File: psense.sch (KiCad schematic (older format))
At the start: 25 parts, among them J1 USB-micro-b, U1 PAC1720, U2 MCP2221A

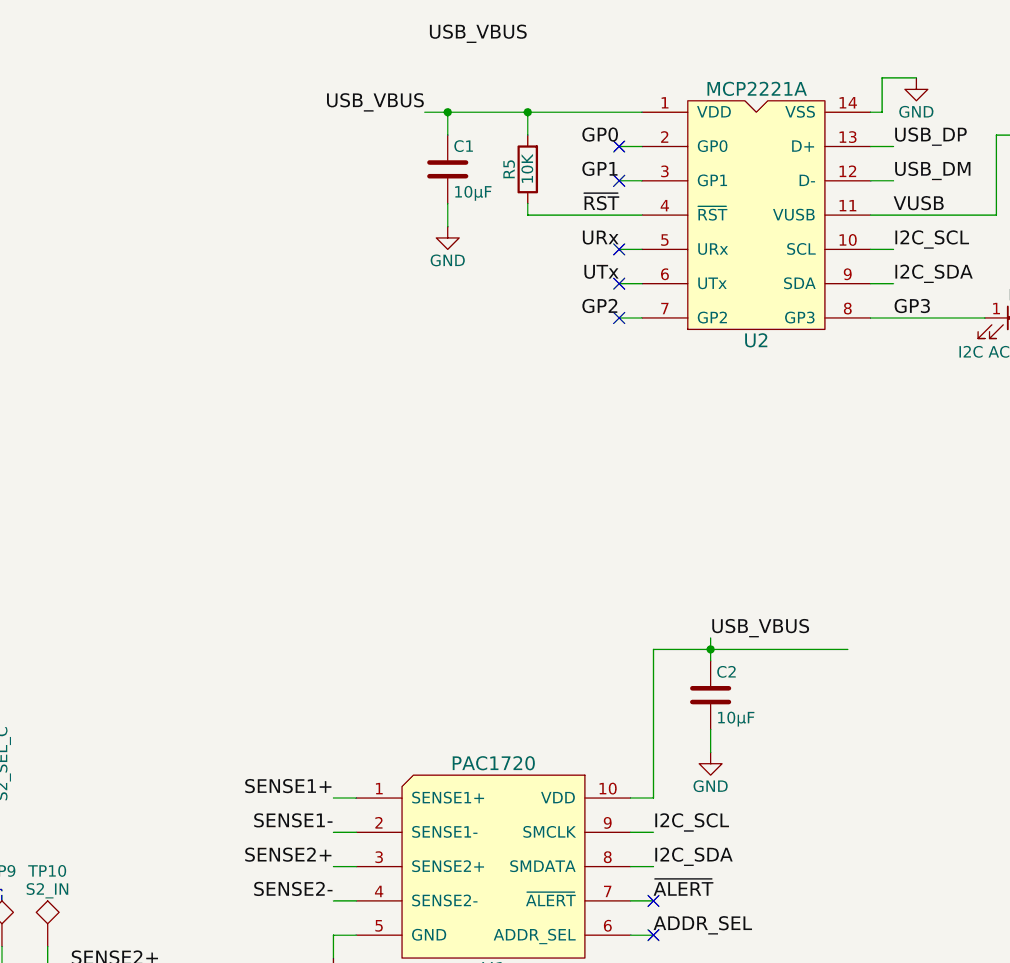
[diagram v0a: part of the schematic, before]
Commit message: Fix https://github.com/noahp/psense/issues/1 https://github.com/noahp/psense/issues/2 https://github.com/noahp/psense/issues/3
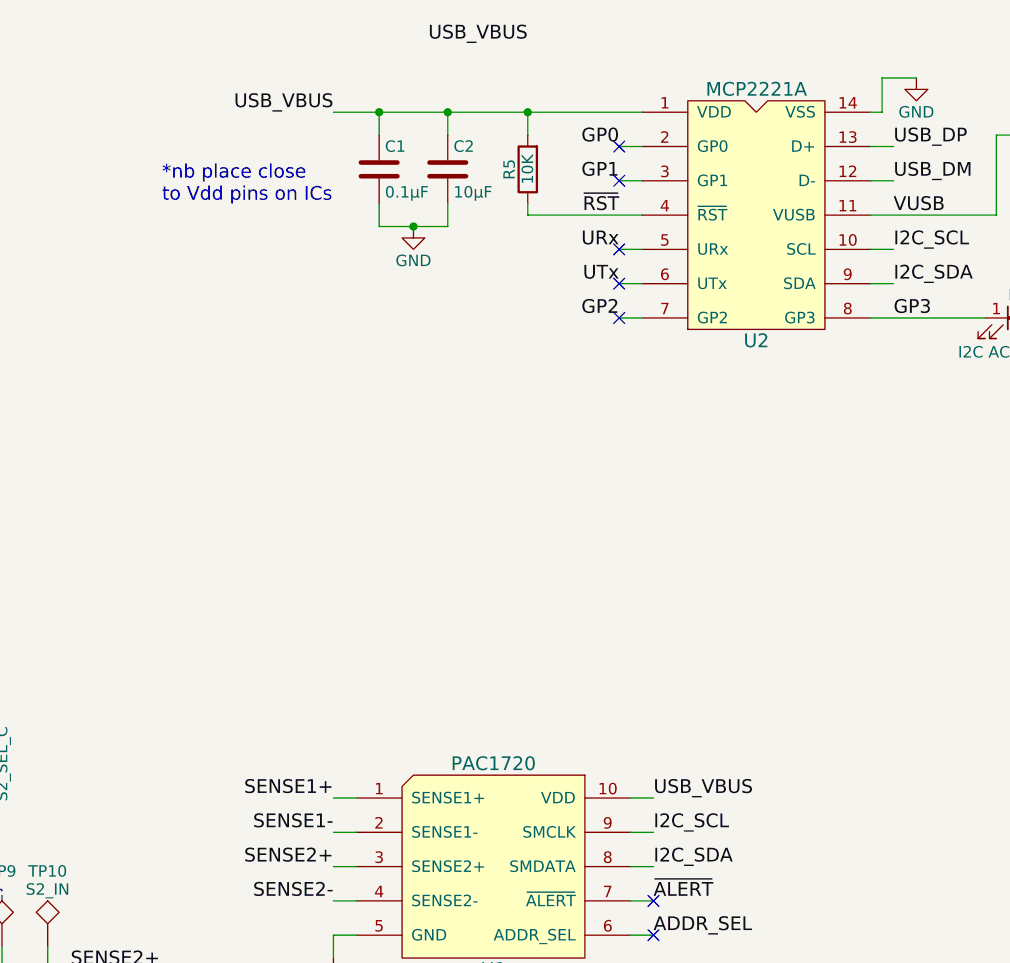
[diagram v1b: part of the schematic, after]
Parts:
- C1: renamed from C2; value 10µF -> 0.1µF
- renumbered C1 to C2
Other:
- note added: "*nb place close\nto Vdd pins on ICs"
- moved on the sheet: C1
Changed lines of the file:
@@
 $EndComp
 $Comp
-L GND #PWR01
+L GND #PWR1
 U 1 1 58A0804C
 P 2700 2700
-F 0 "#PWR01" H 2700 2450 50  0001 C CNN
+F 0 "#PWR1" H 2700 2450 50  0001 C CNN
 F 1 "GND" H 2700 2550 50  0000 C CNN
 F 2 "" H 2700 2700 50  0000 C CNN
@@
 $EndComp
 $Comp
-L GND #PWR02
+L GND #PWR2
 U 1 1 58A09C3A
 P 5150 5200
-F 0 "#PWR02" H 5150 4950 50  0001 C CNN
+F 0 "#PWR2" H 5150 4950 50  0001 C CNN
 F 1 "GND" H 5150 5050 50  0000 C CNN
 F 2 "" H 5150 5200 50  0000 C CNN
@@
 Wire Wire Line
 	6450 4800 6550 4800
-Text Label 6800 3800 0    60   ~ 0
+Text Label 6550 4500 0    60   ~ 0
 USB_VBUS
 $Comp
-L C C2
+L C C1
 U 1 1 58A0A596
-P 6800 4050
-F 0 "C2" H 6825 4150 50  0000 L CNN
-F 1 "10µF" H 6825 3950 50  0000 L CNN
-F 2 "kicadlib:SMD_0603_C" H 6838 3900 50  0001 C CNN
-F 3 "" H 6800 4050 50  0000 C CNN
-	1    6800 4050
-	1    0    0    -1
-$EndComp
-$Comp
-L GND #PWR03
-U 1 1 58A0A5DF
-P 6800 4300
-F 0 "#PWR03" H 6800 4050 50  0001 C CNN
-F 1 "GND" H 6800 4150 50  0000 C CNN
-F 2 "" H 6800 4300 50  0000 C CNN
-F 3 "" H 6800 4300 50  0000 C CNN
-	1    6800 4300
-	1    0    0    -1
-$EndComp
-Wire Wire Line
-	6800 4300 6800 4200
-Wire Wire Line
-	6800 3800 6800 3900
-Wire Wire Line
-	6550 3850 6550 4500
+P 5350 1750
+F 0 "C1" H 5375 1850 50  0000 L CNN
+F 1 "0.1µF" H 5375 1650 50  0000 L CNN
+F 2 "kicadlib:SMD_0603_C" H 5388 1600 50  0001 C CNN
+F 3 "" H 5350 1750 50  0000 C CNN
+	1    5350 1750
+	1    0    0    -1
+$EndComp
 Wire Wire Line
 	6550 4500 6450 4500
-Connection ~ 6800 3850
-Wire Wire Line
-	6550 3850 7400 3850
 $Comp
 L LED D1
@@
 	9100 2400 8800 2400
 $Comp
-L GND #PWR04
+L GND #PWR4
 U 1 1 58A0B59A
 P 7700 1350
-F 0 "#PWR04" H 7700 1100 50  0001 C CNN
+F 0 "#PWR4" H 7700 1100 50  0001 C CNN
 F 1 "GND" H 7700 1200 50  0000 C CNN
 F 2 "" H 7700 1350 50  0000 C CNN
@@
 $EndComp
 $Comp
-L GND #PWR05
+L GND #PWR5
 U 1 1 58A0BB70
 P 8250 2050
-F 0 "#PWR05" H 8250 1800 50  0001 C CNN
+F 0 "#PWR5" H 8250 1800 50  0001 C CNN
 F 1 "GND" H 8250 1900 50  0000 C CNN
 F 2 "" H 8250 2050 50  0000 C CNN
@@
 	6500 2400 6400 2400
 $Comp
-L C C1
+L C C2
 U 1 1 58A1026C
 P 5650 1750
-F 0 "C1" H 5675 1850 50  0000 L CNN
+F 0 "C2" H 5675 1850 50  0000 L CNN
 F 1 "10µF" H 5675 1650 50  0000 L CNN
 F 2 "kicadlib:SMD_0603_C" H 5688 1600 50  0001 C CNN
@@
 	1    0    0    -1
 $EndComp
-Text Label 5550 1500 2    60   ~ 0
+Text Label 5150 1500 2    60   ~ 0
 USB_VBUS
 Wire Wire Line
-	5550 1500 6500 1500
+	5150 1500 6500 1500
 Wire Wire Line
 	5650 1500 5650 1600
 Connection ~ 5650 1500
 $Comp
-L GND #PWR06
+L GND #PWR3
 U 1 1 58A1064D
-P 5650 2000
-F 0 "#PWR06" H 5650 1750 50  0001 C CNN
-F 1 "GND" H 5650 1850 50  0000 C CNN
-F 2 "" H 5650 2000 50  0000 C CNN
-F 3 "" H 5650 2000 50  0000 C CNN
-	1    5650 2000
+P 5500 2000
+F 0 "#PWR3" H 5500 1750 50  0001 C CNN
+F 1 "GND" H 5500 1850 50  0000 C CNN
+F 2 "" H 5500 2000 50  0000 C CNN
+F 3 "" H 5500 2000 50  0000 C CNN
+	1    5500 2000
 	1    0    0    -1
 $EndComp
@@
 	6450 4950 6550 4950
 NoConn ~ 6550 4950
+Wire Wire Line
+	5350 1600 5350 1500
+Connection ~ 5350 1500
+Wire Wire Line
+	5350 1900 5350 2000
+Wire Wire Line
+	5350 2000 5650 2000
+Connection ~ 5500 2000
+Text Notes 4400 1900 0    60   ~ 0
+*nb place close\nto Vdd pins on ICs
 $EndSCHEMATC

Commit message: Update render
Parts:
- J1: footprint kicadlib:usb_micro_b_smt -> kicadlib:SMD_MICRO_USB_B_WPEGS
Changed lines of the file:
@@
 F 0 "J1" H 2150 1800 60  0000 C CNN
 F 1 "USB-micro-b" H 2150 3050 60  0000 C CNN
-F 2 "kicadlib:usb_micro_b_smt" H 2150 2400 60  0001 C CNN
+F 2 "kicadlib:SMD_MICRO_USB_B_WPEGS" H 2150 2400 60  0001 C CNN
 F 3 "" H 2150 2400 60  0000 C CNN
 	1    2150 2400
@@
 $EndComp
 $Comp
-L GND #PWR1
+L GND #PWR01
 U 1 1 58A0804C
 P 2700 2700
-F 0 "#PWR1" H 2700 2450 50  0001 C CNN
+F 0 "#PWR01" H 2700 2450 50  0001 C CNN
 F 1 "GND" H 2700 2550 50  0000 C CNN
 F 2 "" H 2700 2700 50  0000 C CNN
@@
 $EndComp
 $Comp
-L GND #PWR2
+L GND #PWR02
 U 1 1 58A09C3A
 P 5150 5200
-F 0 "#PWR2" H 5150 4950 50  0001 C CNN
+F 0 "#PWR02" H 5150 4950 50  0001 C CNN
 F 1 "GND" H 5150 5050 50  0000 C CNN
 F 2 "" H 5150 5200 50  0000 C CNN
@@
 	9100 2400 8800 2400
 $Comp
-L GND #PWR4
+L GND #PWR03
 U 1 1 58A0B59A
 P 7700 1350
-F 0 "#PWR4" H 7700 1100 50  0001 C CNN
+F 0 "#PWR03" H 7700 1100 50  0001 C CNN
 F 1 "GND" H 7700 1200 50  0000 C CNN
 F 2 "" H 7700 1350 50  0000 C CNN
@@
 $EndComp
 $Comp
-L GND #PWR5
+L GND #PWR04
 U 1 1 58A0BB70
 P 8250 2050
-F 0 "#PWR5" H 8250 1800 50  0001 C CNN
+F 0 "#PWR04" H 8250 1800 50  0001 C CNN
 F 1 "GND" H 8250 1900 50  0000 C CNN
 F 2 "" H 8250 2050 50  0000 C CNN
@@
 Connection ~ 5650 1500
 $Comp
-L GND #PWR3
+L GND #PWR05
 U 1 1 58A1064D
 P 5500 2000
-F 0 "#PWR3" H 5500 1750 50  0001 C CNN
+F 0 "#PWR05" H 5500 1750 50  0001 C CNN
 F 1 "GND" H 5500 1850 50  0000 C CNN
 F 2 "" H 5500 2000 50  0000 C CNN

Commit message: Use FT200XD instead
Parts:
- removed C1: 0.1µF, kicadlib:SMD_0603_C, symbol C
- removed C2: 10µF, kicadlib:SMD_0603_C, symbol C
- removed C3: 0.22-0.47µF, kicadlib:SMD_0603_C, symbol C
- removed D1: I2C ACTIVE LED, kicadlib:SMD_0603_LED_REVERSED, symbol LED
- removed J1: USB-micro-b, kicadlib:SMD_MICRO_USB_B_WPEGS, symbol USB-micro-b
- removed R1, R3: 0.1R, kicadlib:SMD_0603_R, symbol R
- removed R2, R4: 1.0R, kicadlib:SMD_0603_R, symbol R
- removed R5: 10K, kicadlib:SMD_0603_R, symbol R
- removed R6: 1K, kicadlib:SMD_0603_R, symbol R
- removed R7, R8: 4.7K, kicadlib:SMD_0603_R, symbol R
- removed TP1: S1_OUT, kicadlib:TEST_0.100, symbol TEST
- removed TP10: S2_IN, kicadlib:TEST_0.100, symbol TEST
- removed TP2: S1_SEL_H, kicadlib:TEST_0.100, symbol TEST
- removed TP3: S1_SEL_L, kicadlib:TEST_0.100, symbol TEST
- removed TP4: S1_SEL_C, kicadlib:TEST_0.100, symbol TEST
- removed TP5: S1_IN, kicadlib:TEST_0.100, symbol TEST
- removed TP6: S2_OUT, kicadlib:TEST_0.100, symbol TEST
- removed TP7: S2_SEL_H, kicadlib:TEST_0.100, symbol TEST
- removed TP8: S2_SEL_L, kicadlib:TEST_0.100, symbol TEST
- removed TP9: S2_SEL_C, kicadlib:TEST_0.100, symbol TEST
- removed U1: PAC1720, kicadlib:SMD_10-DFN, symbol PAC1720
- removed U2: MCP2221A, kicadlib:SMD_14-SOIC, symbol MCP2221A
- added C1: 0.1µF, Capacitor_SMD:C_0603_1608Metric, symbol Device:C
- added C2: 10pF, Capacitor_SMD:C_0603_1608Metric, symbol Device:C
- added C3: 100nF, Capacitor_SMD:C_0603_1608Metric, symbol Device:C
- added J1: USB_B_Micro, Connector_USB:USB_Micro-B_Molex_47346-0001, symbol Connector:USB_B_Micro
- added R1, R3: 0.1R, Resistor_SMD:R_0603_1608Metric, symbol Device:R
- added R2, R4: 1.0R, Resistor_SMD:R_0603_1608Metric, symbol Device:R
- added R5, R6: 1K, Resistor_SMD:R_0603_1608Metric, symbol Device:R
- added TP1: S1_OUT, Connector_PinHeader_2.54mm:PinHeader_1x01_P2.54mm_Horizontal, symbol Connector:TestPoint
- added TP10: S2_IN, Connector_PinHeader_2.54mm:PinHeader_1x01_P2.54mm_Horizontal, symbol Connector:TestPoint
- added TP2: S1_SEL_H, Connector_PinHeader_2.54mm:PinHeader_1x01_P2.54mm_Horizontal, symbol Connector:TestPoint
- added TP3: S1_SEL_L, Connector_PinHeader_2.54mm:PinHeader_1x01_P2.54mm_Horizontal, symbol Connector:TestPoint
- added TP4: S1_SEL_C, Connector_PinHeader_2.54mm:PinHeader_1x01_P2.54mm_Horizontal, symbol Connector:TestPoint
- added TP5: S1_IN, Connector_PinHeader_2.54mm:PinHeader_1x01_P2.54mm_Horizontal, symbol Connector:TestPoint
- added TP6: S2_OUT, Connector_PinHeader_2.54mm:PinHeader_1x01_P2.54mm_Horizontal, symbol Connector:TestPoint
- added TP7: S2_SEL_H, Connector_PinHeader_2.54mm:PinHeader_1x01_P2.54mm_Horizontal, symbol Connector:TestPoint
- added TP8: S2_SEL_L, Connector_PinHeader_2.54mm:PinHeader_1x01_P2.54mm_Horizontal, symbol Connector:TestPoint
- added TP9: S2_SEL_C, Connector_PinHeader_2.54mm:PinHeader_1x01_P2.54mm_Horizontal, symbol Connector:TestPoint
- added U1: PAC1720, Package_DFN_QFN:DFN-10-1EP_2x3mm_P0.5mm_EP0.64x2.4mm, symbol kicadlib:PAC1720
- added U2: FT200XD, Package_DFN_QFN:DFN-10-1EP_3x3mm_P0.5mm_EP1.55x2.48mm, symbol Interface_USB:FT200XD
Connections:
- net labels added: FT200XD_VCCIO
- net labels removed: GP0, GP1, GP2, GP3, URx, UTx, VUSB, ~RST
- wire segments 70 -> 71
- no-connect marks 9 -> 5
